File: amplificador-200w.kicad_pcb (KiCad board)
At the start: 2 copper layers, 92.5 x 81 mm, 36 parts, among them J1 IN, J10 MH, J11 MH, J12 FAN, J2 AUX, J3 PWR, J4 out, J5 out, J6 out, J7 out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

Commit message: actualizando circuito
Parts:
- moved C9 33.9 mm to (125.6, 100.2), turned to 180 degrees
- moved G*** 9.05 mm to (157.0, 71.7)
- moved C1 1.36 mm to (125.5, 97.6)
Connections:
- J3 pad 1: GND -> /REMOTE
- J3 pad 3: /REMOTE -> GND
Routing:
- net GND: track 277.6 -> 6.64 mm, vias 2 -> 0
- net Net-(U1-AC-GND): track 19.3 -> 30.0 mm
- net /REMOTE: track 71.3 -> 62.2 mm
- net Net-(U1-MUTE): track 38.1 -> 43.5 mm
- net VCC: track 308.1 -> 313.2 mm, vias 0 -> 2
- net Net-(U1-IN4): track 31.8 -> 28.4 mm
- net Net-(D1-A): track 24.2 -> 27.3 mm
- net Net-(U1-ST-BY): track 35.2 -> 37.1 mm
- net Net-(U1-IN3): track 35.8 -> 34.3 mm
- net Net-(J1-Pin_4): track 24.9 -> 25.6 mm
- net Net-(J1-Pin_2): track 18.6 -> 19.1 mm
- removed copper zone on F.Cu, net GND
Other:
- net class Default removed

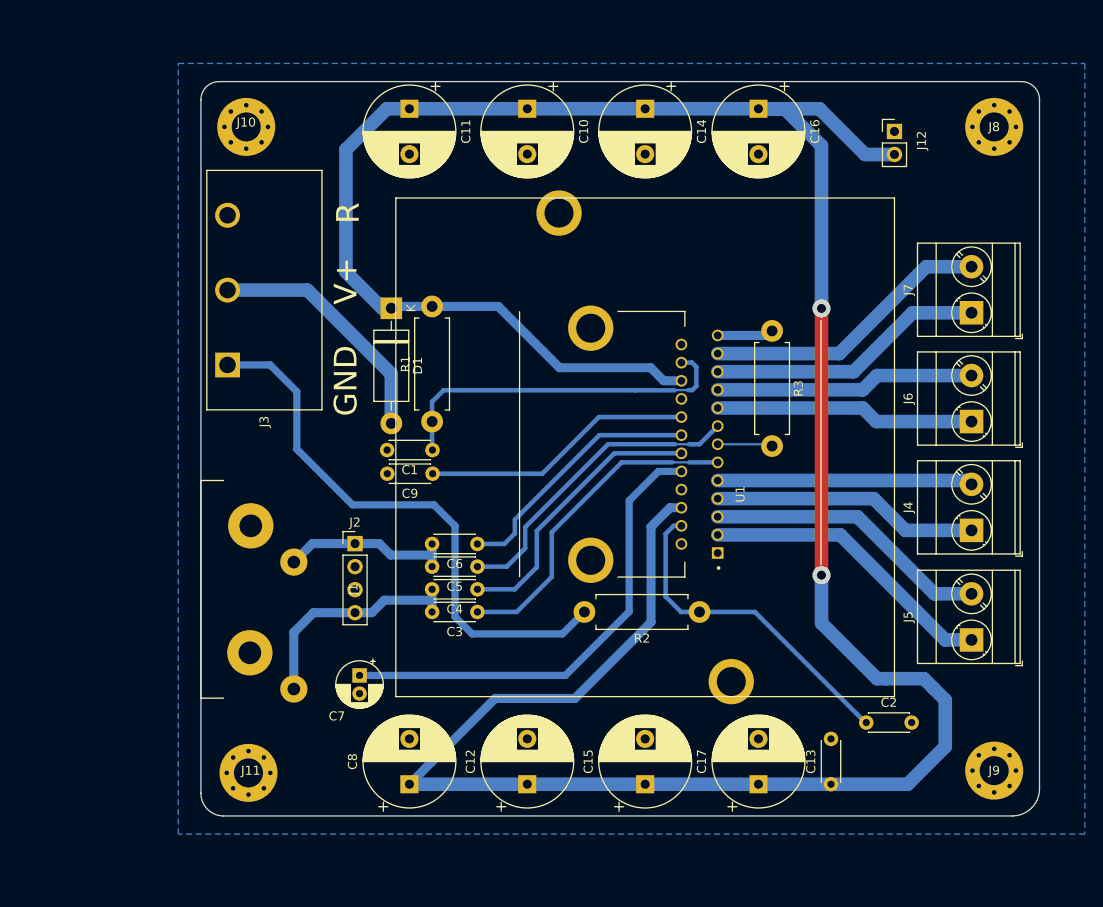
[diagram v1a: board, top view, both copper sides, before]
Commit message: quitando la entrada de audio auxiliar
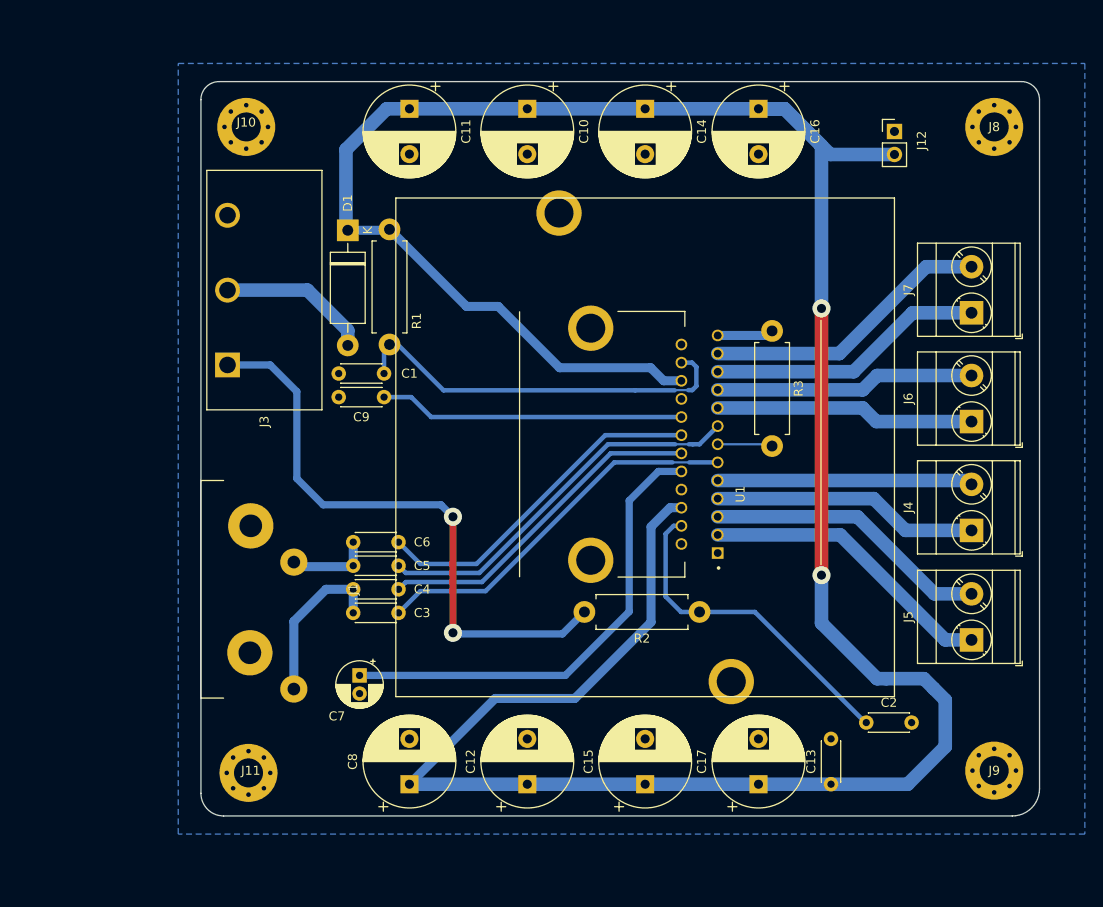
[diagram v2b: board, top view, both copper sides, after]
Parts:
- removed G***: LOGO, MSS_Devices:logo-mr
- removed J2: AUX, Connector_PinHeader_2.54mm:PinHeader_1x04_P2.54mm_Vertical
- moved C9 10.0 mm to (120.2, 91.8)
- moved C1 9.99 mm to (120.2, 89.2)
- moved D1 9.85 mm to (116.2, 73.4)
- moved R1 9.71 mm to (120.8, 86.0)
- moved C6 8.70 mm to (121.8, 107.8)
- moved C3 8.70 mm to (121.8, 115.6)
- moved C5 8.70 mm to (121.8, 110.4)
- moved C4 8.70 mm to (121.8, 113.0)
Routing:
- net Net-(D1-A): track 27.3 -> 16.8 mm
- net Net-(J1-Pin_2): track 19.1 -> 9.40 mm
- net Net-(U1-IN4): track 28.4 -> 38.1 mm
- net Net-(U1-IN3): track 34.3 -> 42.2 mm
- net Net-(J1-Pin_4): track 25.6 -> 18.1 mm
- net Net-(U1-IN2): track 31.1 -> 37.4 mm
- net Net-(U1-IN1): track 36.2 -> 42.1 mm
- net Net-(U1-MUTE): track 43.5 -> 47.9 mm
- net Net-(U1-AC-GND): track 30.0 -> 33.7 mm
- net /REMOTE: track 62.2 -> 65.8 mm, vias 0 -> 2
- net VCC: track 313.2 -> 310.4 mm
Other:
- board text removed: "GND"
- board text removed: "R"
- board text removed: "V+"

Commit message: version 2 enviada a fabricar
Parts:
- added C18: 100nF, Capacitor_SMD:C_0603_1608Metric_Pad1.08x0.95mm_HandSolder, B.Cu at (150.2, 90.0)
- added D2: D_ALT, Diode_SMD:D_SMA, B.Cu at (117.2, 79.8)
- added D3: LED, LED_THT:LED_D3.0mm, F.Cu at (117.6, 55.3)
- added G***: LOGO, MR-footprint:logo_mr_6x6mm, F.Cu at (142.4, 141.2)
- added R4: 10K, Resistor_SMD:R_0603_1608Metric, B.Cu at (115.8, 62.4)
- added RV1: R_Potentiometer_Dual, Potentiometer_THT:Potentiometer_Alps_RK097_Dual_Horizontal, F.Cu at (105.0, 95.5)
- C1, C2: footprint Capacitor_THT:C_Disc_D4.3mm_W1.9mm_P5.00mm -> Capacitor_SMD:C_0805_2012Metric; moved to B.Cu
- C13, C3, C4, C5, C6: value 0.1uF -> 100nF; footprint Capacitor_THT:C_Disc_D4.3mm_W1.9mm_P5.00mm -> Capacitor_SMD:C_0603_1608Metric_Pad1.08x0.95mm_HandSolder; moved to B.Cu
- C9: footprint Capacitor_THT:C_Disc_D4.3mm_W1.9mm_P5.00mm -> Capacitor_SMD:C_0603_1608Metric_Pad1.08x0.95mm_HandSolder; moved to B.Cu
- D1: footprint Diode_THT:D_DO-15_P12.70mm_Horizontal -> Diode_SMD:D_SMA; moved to B.Cu
- J12: footprint Connector_PinHeader_2.54mm:PinHeader_1x02_P2.54mm_Vertical -> Connector_JST:JST_PH_B2B-PH-K_1x02_P2.00mm_Vertical
- R1, R2, R3: footprint Resistor_THT:R_Axial_DIN0411_L9.9mm_D3.6mm_P12.70mm_Horizontal -> Resistor_SMD:R_0603_1608Metric; moved to B.Cu
- moved C13 36.4 mm to (151.0, 103.2)
- moved C9 30.6 mm to (150.8, 93.2), turned to 90 degrees
- moved R1 30.3 mm to (151.1, 85.4)
- moved C1 29.9 mm to (150.1, 88.0)
- moved C2 29.6 mm to (150.8, 108.6), turned to -90 degrees
- moved C7 18.7 mm to (113.8, 104.1)
- moved C3 13.6 mm to (121.5, 102.0)
- moved C4 12.5 mm to (121.5, 100.5)
- moved J9 12.0 mm to (179.0, 141.5)
- moved C5 11.4 mm to (121.5, 99.0)
- moved J8 11.3 mm to (179.0, 54.5)
- moved J1 11.0 mm to (105.5, 124.0)
- moved R2 10.8 mm to (149.9, 106.0)
- moved C6 10.3 mm to (121.5, 97.5)
- moved J11 8.34 mm to (104.0, 141.5)
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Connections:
- net VCC renamed +12V
- C3 pad 2: Net-(J1-Pin_4) -> /IN_LEFT_P
- C4 pad 2: Net-(J1-Pin_4) -> /IN_LEFT_P
- C5 pad 2: Net-(J1-Pin_2) -> /IN_RIGTH_P
- C6 pad 2: Net-(J1-Pin_2) -> /IN_RIGTH_P
- J1 pad 2: Net-(J1-Pin_2) -> /IN_RIGTH
- J1 pad 4: Net-(J1-Pin_4) -> /IN_LEFT
- J3 pad 1: /REMOTE -> Net-(D2-A)
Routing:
- net Net-(U1-MUTE): track 47.9 -> 3.76 mm
- net /IN_LEFT: track 0.00 -> 39.0 mm
- net +12V: track 310.4 -> 273.7 mm
- net Net-(U1-ST-BY): track 37.1 -> 3.91 mm
- net Net-(U1-AC-GND): track 33.7 -> 2.30 mm
- net /IN_RIGTH_P: track 0.00 -> 24.5 mm
- net /IN_RIGTH: track 0.00 -> 22.7 mm
- net /IN_LEFT_P: track 0.00 -> 21.4 mm
- net Net-(J1-Pin_4): track 18.1 -> 0.00 mm
- net Net-(D2-A): track 0.00 -> 12.4 mm
- net Net-(U1-SVR): track 52.0 -> 40.9 mm
- net /REMOTE: track 65.8 -> 56.2 mm
- net Net-(J1-Pin_2): track 9.40 -> 0.00 mm
- net Net-(U1-IN4): track 38.1 -> 31.3 mm
- net GND: track 6.64 -> 0.00 mm
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- added copper zone on F.Cu, net GND
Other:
- board size 92.5 x 81 mm -> 83 x 95 mm
- board text added: "MAYKOLREY.COM ${REVISION}"
- board text removed: "MAYKOLREY.COM"

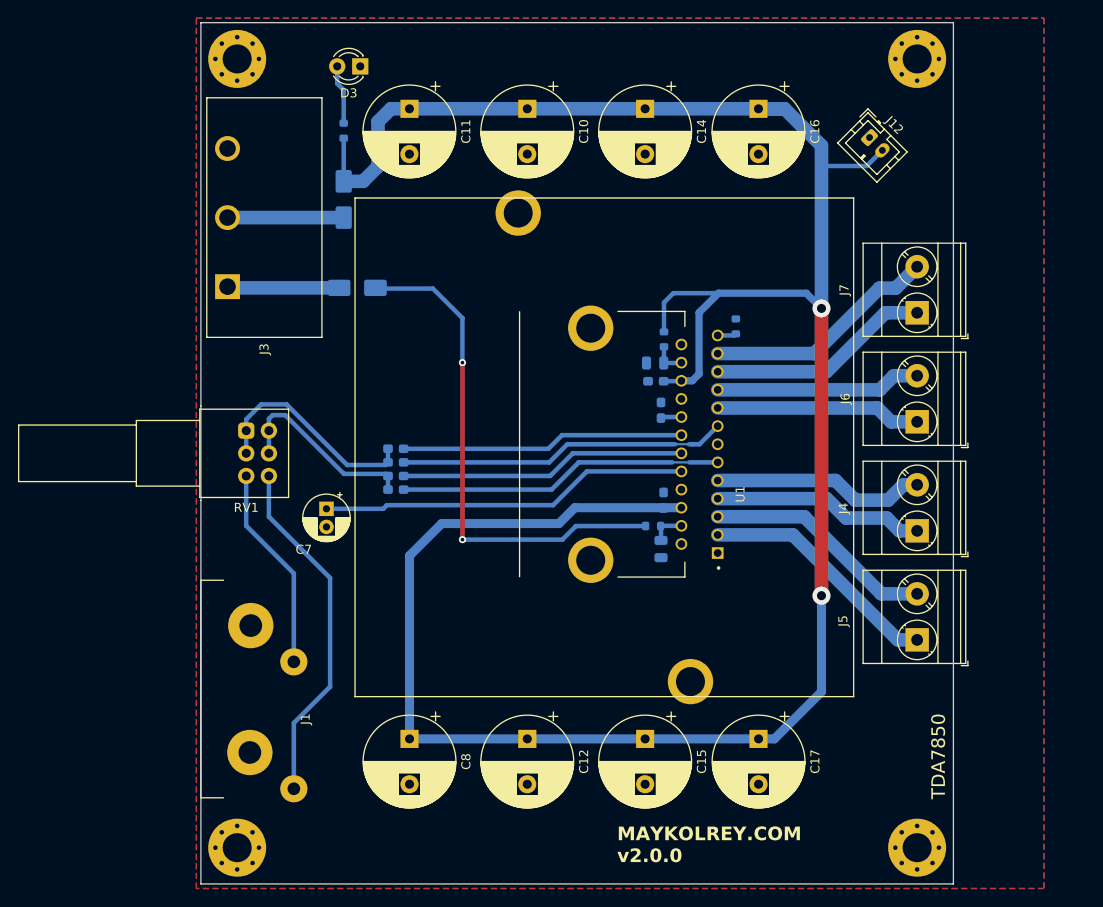
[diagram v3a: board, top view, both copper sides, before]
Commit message: corrgiendo disipador y que el ventilador solo prenda con remote
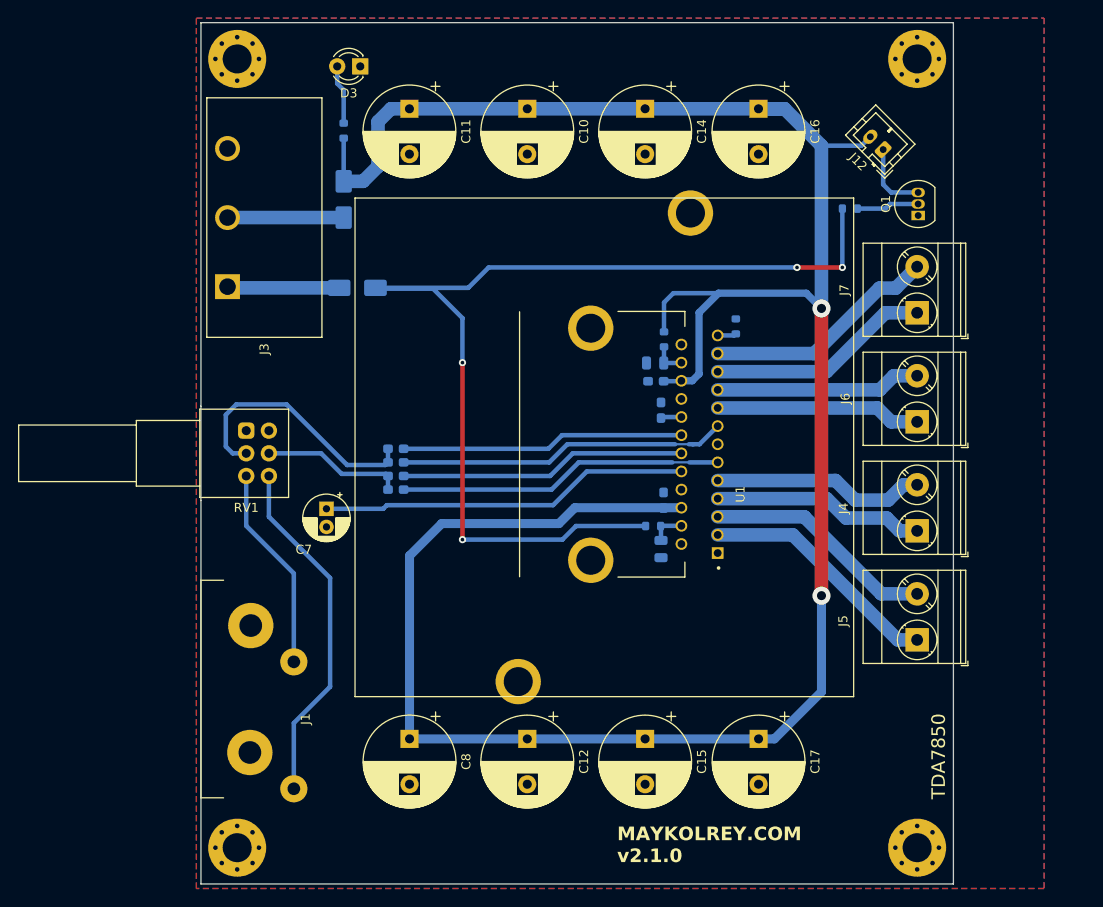
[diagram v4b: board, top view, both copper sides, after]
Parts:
- added Q1: 2N3904, Package_TO_SOT_THT:TO-92_Inline, F.Cu at (179.1, 71.8)
- added R5: 10K, Resistor_SMD:R_0603_1608Metric, B.Cu at (171.6, 71.0)
- moved J12 2.00 mm to (175.2, 64.5), turned to 135 degrees
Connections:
- J12 pad 1: GND -> Net-(J12-Pin_1)
- RV1 pad 1: /IN_RIGTH_P -> GND
- RV1 pad 4: /IN_LEFT_P -> GND
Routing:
- net /REMOTE: track 56.2 -> 115.2 mm, vias 2 -> 4
- net Net-(J12-Pin_1): track 0.00 -> 8.07 mm
- net Net-(Q1-B): track 0.00 -> 6.92 mm
- net /IN_LEFT_P: track 21.4 -> 15.7 mm
- net /IN_RIGTH_P: track 24.5 -> 28.8 mm
- net +12V: track 273.7 -> 270.1 mm
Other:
- rule pad_to_mask_clearance: 0.051 -> 0
